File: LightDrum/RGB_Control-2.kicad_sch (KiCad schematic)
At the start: 25 parts, among them U401 PCA9634_TSSOP20, U402 SQ2310ES_SOT23, U403 SQ2310ES_SOT23, U404 SQ2310ES_SOT23, U405 SQ2310ES_SOT23, U406 SQ2310ES_SOT23, U407 SQ2310ES_SOT23, U408 SQ2310ES_SOT23, U409 SQ2310ES_SOT23

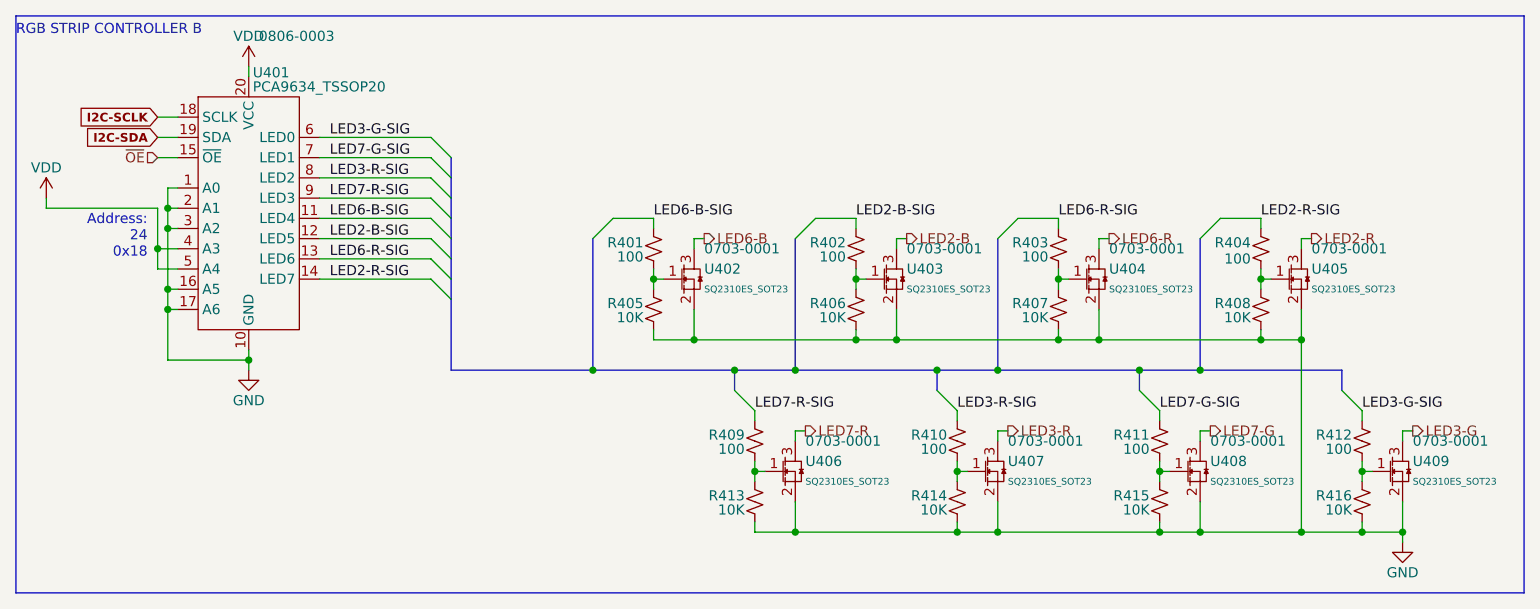
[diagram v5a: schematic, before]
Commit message: Replace old MOSFETs with a more compact package
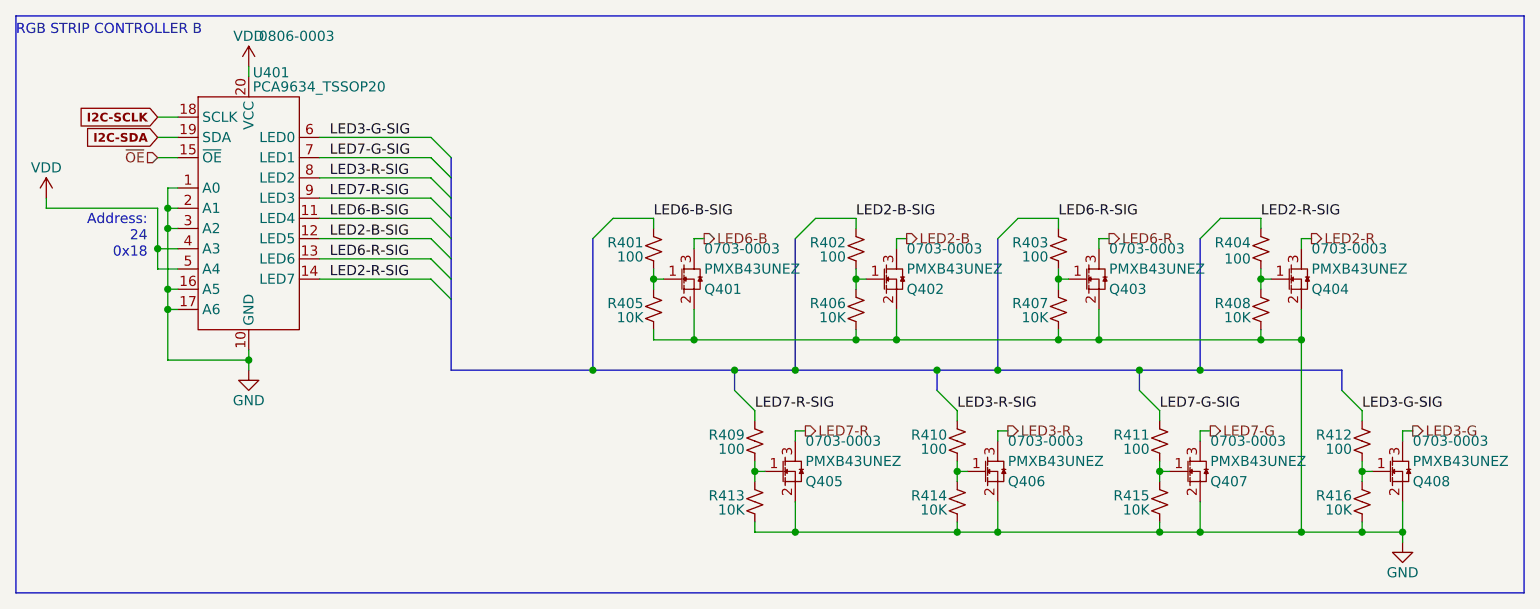
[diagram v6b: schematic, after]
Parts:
- removed U402, U403, U404, U405, U406, U407, U408, U409: SQ2310ES_SOT23, Package_TO_SOT_SMD:SOT-23, symbol Daxxn_Transistors:SQ2310ES_SOT23
- added Q401, Q402, Q403, Q404, Q405, Q406, Q407, Q408: PMXB43UNEZ, Daxxn_Packages:DFN1010D-3, symbol Daxxn_Transistors:PMXB43UNEZ
- R401, R402, R403, R404, R405, R406, R407, R408, R409, R410, R411, R412, R413, R414, R415, R416: footprint Resistor_SMD:R_0805_2012Metric -> Resistor_SMD:R_0603_1608Metric
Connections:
- net GND: now also Q401.2 (S), Q402.2 (S), Q403.2 (S), Q404.2 (S), Q405.2 (S), Q406.2 (S), Q407.2 (S), Q408.2 (S)
- net LED2-B: now also Q402.3 (D)
- net LED2-R: now also Q404.3 (D)
- net LED3-G: now also Q408.3 (D)
- net LED3-R: now also Q406.3 (D)
- net LED6-B: now also Q401.3 (D)
- net LED6-R: now also Q403.3 (D)
- net LED7-G: now also Q407.3 (D)
- net LED7-R: now also Q405.3 (D)
- net at R401.2, R405.1: now also Q401.1 (G)
- net at R404.2, R408.1: now also Q404.1 (G)
- net at R411.2, R415.1: now also Q407.1 (G)
- net at R410.2, R414.1: now also Q406.1 (G)
- net at R412.2, R416.1: now also Q408.1 (G)
- net at R409.2, R413.1: now also Q405.1 (G)
- net at R403.2, R407.1: now also Q403.1 (G)
- net at R402.2, R406.1: now also Q402.1 (G)

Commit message: Lock REV8 Layout and send to PCB MNF
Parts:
- R401, R402, R403, R404, R405, R406, R407, R408, R409, R410, R411, R412, R413, R414, R415, R416: footprint Resistor_SMD:R_0603_1608Metric -> Resistor_SMD:R_0402_1005Metric
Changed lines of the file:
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@@
       (effects (font (size 1.27 1.27)) (justify right))
     )
-    (property "Footprint" "Resistor_SMD:R_0603_1608Metric" (id 2) (at 172.72 53.34 0)
+    (property "Footprint" "Resistor_SMD:R_0402_1005Metric" (id 2) (at 172.72 53.34 0)
       (effects (font (size 1.27 1.27)) hide)
     )
@@
       (effects (font (size 1.27 1.27)) (justify right))
     )
-    (property "Footprint" "Resistor_SMD:R_0603_1608Metric" (id 2) (at 185.42 77.47 0)
+    (property "Footprint" "Resistor_SMD:R_0402_1005Metric" (id 2) (at 185.42 77.47 0)
       (effects (font (size 1.27 1.27)) hide)
     )
@@
       (effects (font (size 1.27 1.27)) (justify right))
     )
-    (property "Footprint" "Resistor_SMD:R_0603_1608Metric" (id 2) (at 172.72 45.72 0)
+    (property "Footprint" "Resistor_SMD:R_0402_1005Metric" (id 2) (at 172.72 45.72 0)
       (effects (font (size 1.27 1.27)) hide)
     )
@@
       (effects (font (size 1.27 1.27)) (justify right))
     )
-    (property "Footprint" "Resistor_SMD:R_0603_1608Metric" (id 2) (at 160.02 69.85 0)
+    (property "Footprint" "Resistor_SMD:R_0402_1005Metric" (id 2) (at 160.02 69.85 0)
       (effects (font (size 1.27 1.27)) hide)
     )
@@
       (effects (font (size 1.27 1.27)) (justify right))
     )
-    (property "Footprint" "Resistor_SMD:R_0603_1608Metric" (id 2) (at 109.22 77.47 0)
+    (property "Footprint" "Resistor_SMD:R_0402_1005Metric" (id 2) (at 109.22 77.47 0)
       (effects (font (size 1.27 1.27)) hide)
     )
@@
       (effects (font (size 1.27 1.27)) (justify right))
     )
-    (property "Footprint" "Resistor_SMD:R_0603_1608Metric" (id 2) (at 147.32 45.72 0)
+    (property "Footprint" "Resistor_SMD:R_0402_1005Metric" (id 2) (at 147.32 45.72 0)
       (effects (font (size 1.27 1.27)) hide)
     )
@@
       (effects (font (size 1.27 1.27)) (justify right))
     )
-    (property "Footprint" "Resistor_SMD:R_0603_1608Metric" (id 2) (at 134.62 69.85 0)
+    (property "Footprint" "Resistor_SMD:R_0402_1005Metric" (id 2) (at 134.62 69.85 0)
       (effects (font (size 1.27 1.27)) hide)
     )
@@
       (effects (font (size 1.27 1.27)) (justify right))
     )
-    (property "Footprint" "Resistor_SMD:R_0603_1608Metric" (id 2) (at 121.92 45.72 0)
+    (property "Footprint" "Resistor_SMD:R_0402_1005Metric" (id 2) (at 121.92 45.72 0)
       (effects (font (size 1.27 1.27)) hide)
     )
@@
       (effects (font (size 1.27 1.27)) (justify right))
     )
-    (property "Footprint" "Resistor_SMD:R_0603_1608Metric" (id 2) (at 147.32 53.34 0)
+    (property "Footprint" "Resistor_SMD:R_0402_1005Metric" (id 2) (at 147.32 53.34 0)
       (effects (font (size 1.27 1.27)) hide)
     )
@@
       (effects (font (size 1.27 1.27)) (justify right))
     )
-    (property "Footprint" "Resistor_SMD:R_0603_1608Metric" (id 2) (at 134.62 77.47 0)
+    (property "Footprint" "Resistor_SMD:R_0402_1005Metric" (id 2) (at 134.62 77.47 0)
       (effects (font (size 1.27 1.27)) hide)
     )
@@
       (effects (font (size 1.27 1.27)) (justify right))
     )
-    (property "Footprint" "Resistor_SMD:R_0603_1608Metric" (id 2) (at 96.52 45.72 0)
+    (property "Footprint" "Resistor_SMD:R_0402_1005Metric" (id 2) (at 96.52 45.72 0)
       (effects (font (size 1.27 1.27)) hide)
     )
@@
       (effects (font (size 1.27 1.27)) (justify right))
     )
-    (property "Footprint" "Resistor_SMD:R_0603_1608Metric" (id 2) (at 109.22 69.85 0)
+    (property "Footprint" "Resistor_SMD:R_0402_1005Metric" (id 2) (at 109.22 69.85 0)
       (effects (font (size 1.27 1.27)) hide)
     )
@@
       (effects (font (size 1.27 1.27)) (justify right))
     )
-    (property "Footprint" "Resistor_SMD:R_0603_1608Metric" (id 2) (at 160.02 77.47 0)
+    (property "Footprint" "Resistor_SMD:R_0402_1005Metric" (id 2) (at 160.02 77.47 0)
       (effects (font (size 1.27 1.27)) hide)
     )
@@
       (effects (font (size 1.27 1.27)) (justify right))
     )
-    (property "Footprint" "Resistor_SMD:R_0603_1608Metric" (id 2) (at 121.92 53.34 0)
+    (property "Footprint" "Resistor_SMD:R_0402_1005Metric" (id 2) (at 121.92 53.34 0)
       (effects (font (size 1.27 1.27)) hide)
     )
@@
       (effects (font (size 1.27 1.27)) (justify right))
     )
-    (property "Footprint" "Resistor_SMD:R_0603_1608Metric" (id 2) (at 185.42 69.85 0)
+    (property "Footprint" "Resistor_SMD:R_0402_1005Metric" (id 2) (at 185.42 69.85 0)
       (effects (font (size 1.27 1.27)) hide)
     )
@@
       (effects (font (size 1.27 1.27)) (justify right))
     )
-    (property "Footprint" "Resistor_SMD:R_0603_1608Metric" (id 2) (at 96.52 53.34 0)
-      (effects (font (size 1.27 1.27)) hide)
-    )
+    (property "Footprint" "Resistor_SMD:R_0402_1005Metric" (id 2) (at 96.52 53.34 0)
+      (effects (font (size 1.27 1.27)) hide)
+    )
